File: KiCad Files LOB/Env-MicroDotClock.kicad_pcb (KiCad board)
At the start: 2 copper layers, 90 x 65.2 mm, 331 parts, among them IC1 IS31FL3730-QFLS2-TR, IC2 IS31FL3730-QFLS2-TR, IC3 IS31FL3730-QFLS2-TR, IC4 IS31FL3730-QFLS2-TR, J1 Conn_01x06_Pin, Q1 2SC1815, SW1 SW_SPST, SW2 SW_SPST, SW3 SW_SPST, SW4 SW_SPST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

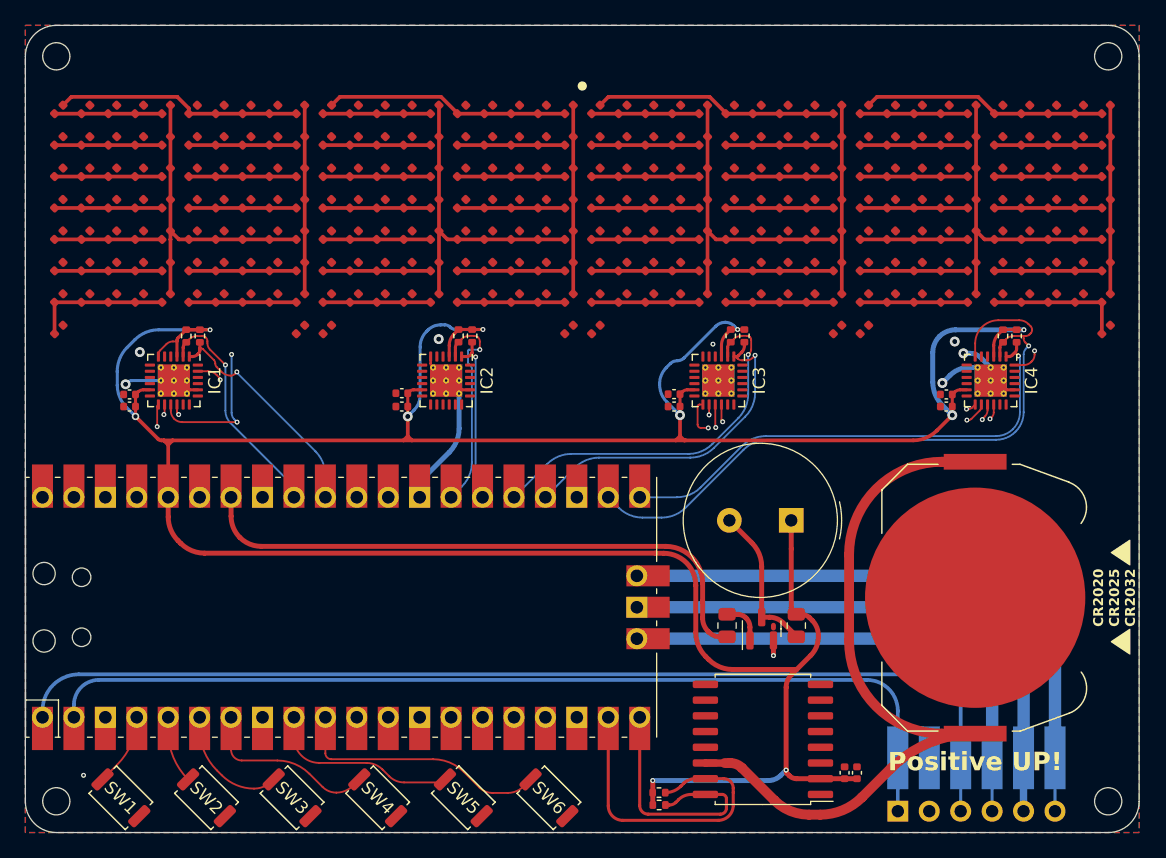
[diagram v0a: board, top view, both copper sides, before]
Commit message: begin autorouter
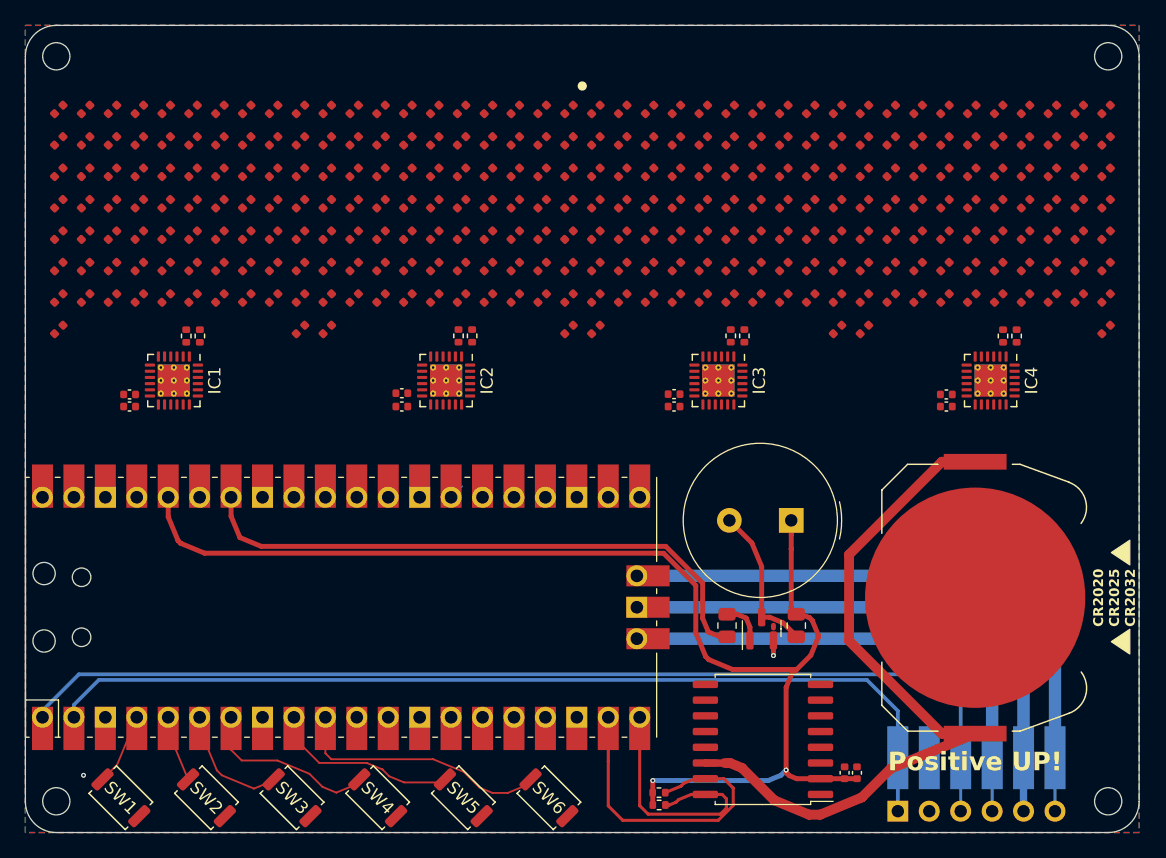
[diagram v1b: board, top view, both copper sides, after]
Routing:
- net +3V3: track 266.6 -> 104.3 mm, vias 10 -> 2
- net I2C4_SCL: track 55.2 -> 0.00 mm, vias 1 -> 0
- net I2C4_SDA: track 40.4 -> 0.00 mm, vias 1 -> 0
- net GND: track 34.7 -> 3.22 mm, vias 9 -> 2
- net I2C3_SCL: track 30.4 -> 0.00 mm, vias 1 -> 0
- net I2C3_SDA: track 27.2 -> 0.00 mm, vias 1 -> 0
- net IC1C5: track 25.7 -> 0.00 mm
- net IC4C5: track 25.7 -> 0.00 mm
- net IC2C5: track 25.7 -> 0.00 mm
- net IC3C5: track 25.7 -> 0.00 mm
- net IC4R5: track 23.9 -> 0.00 mm
- net IC2R5: track 23.9 -> 0.00 mm
- net IC1R5: track 23.9 -> 0.00 mm
- net IC3R5: track 23.9 -> 0.00 mm
- net IC4C1: track 22.1 -> 0.00 mm, vias 1 -> 0
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
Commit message: Fully wired V1 LOB
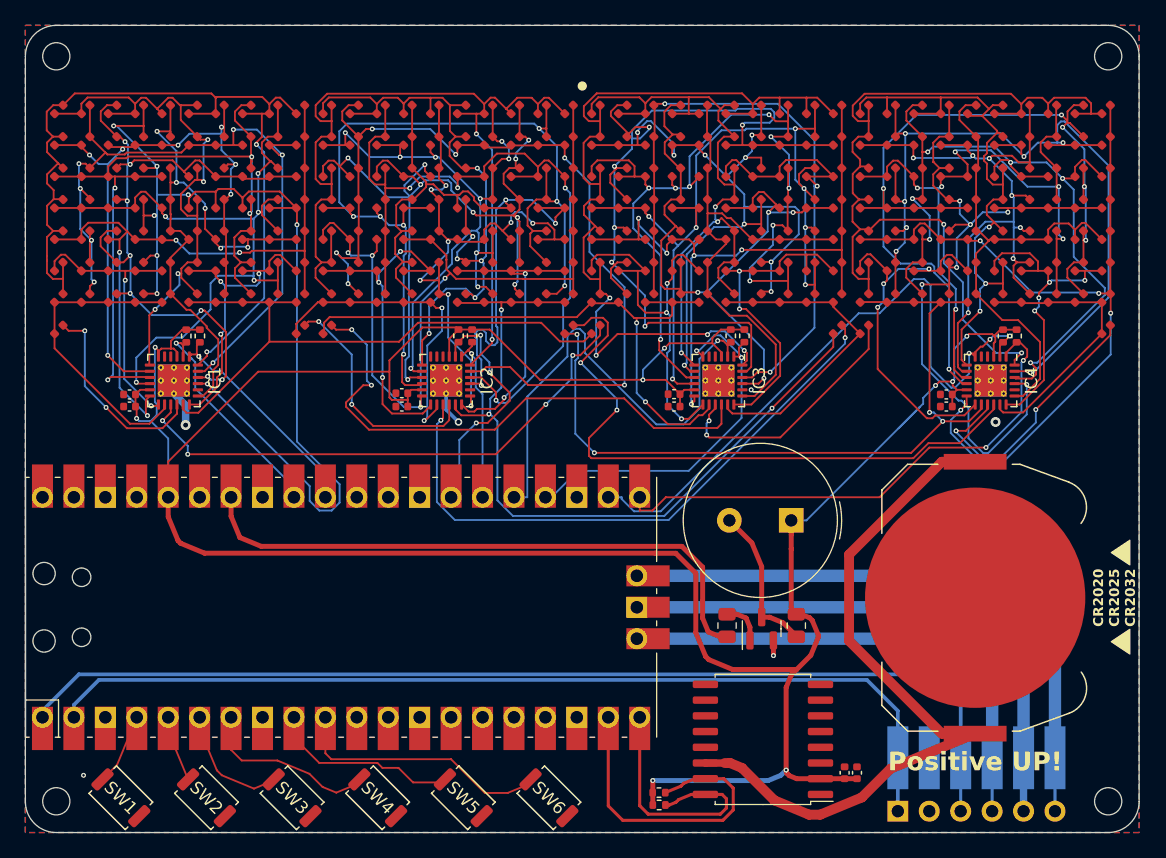
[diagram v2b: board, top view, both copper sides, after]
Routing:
- net +3V3: track 104.3 -> 237.3 mm, vias 2 -> 9
- net IC1C4: track 0.00 -> 87.1 mm, vias 0 -> 8
- net IC2R4: track 0.00 -> 80.2 mm, vias 0 -> 7
- net IC2C1: track 0.00 -> 74.9 mm, vias 0 -> 2
- net IC3C2: track 0.00 -> 74.4 mm, vias 0 -> 6
- net IC4C1: track 0.00 -> 74.2 mm, vias 0 -> 2
- net IC4R4: track 0.00 -> 74.1 mm, vias 0 -> 6
- net IC3C1: track 0.00 -> 73.7 mm, vias 0 -> 4
- net IC2C2: track 0.00 -> 73.5 mm, vias 0 -> 6
- net IC1C1: track 0.00 -> 73.5 mm, vias 0 -> 2
- net IC4C2: track 0.00 -> 70.9 mm, vias 0 -> 7
- net IC3R3: track 0.00 -> 70.9 mm, vias 0 -> 9
- net IC2R3: track 0.00 -> 70.0 mm, vias 0 -> 9
- net IC3C3: track 0.00 -> 67.6 mm, vias 0 -> 3
- net IC3R4: track 0.00 -> 67.4 mm, vias 0 -> 7
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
